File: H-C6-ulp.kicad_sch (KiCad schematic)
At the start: 59 parts, among them J1 USB_C_Receptacle_USB2.0, J2 AFC24-S24FIC-00, J3 S2B-PH-SM4-TB_LF__SN_, Q1 Si1308, Q2 Si2301CDS, U1 ESP32-C6, U2 SGM6029CYG/TR, U3 TP4057-42-SOT26-R, X1 Crystal 40 Mhz 10ppm, Y1 RV-3032-C7

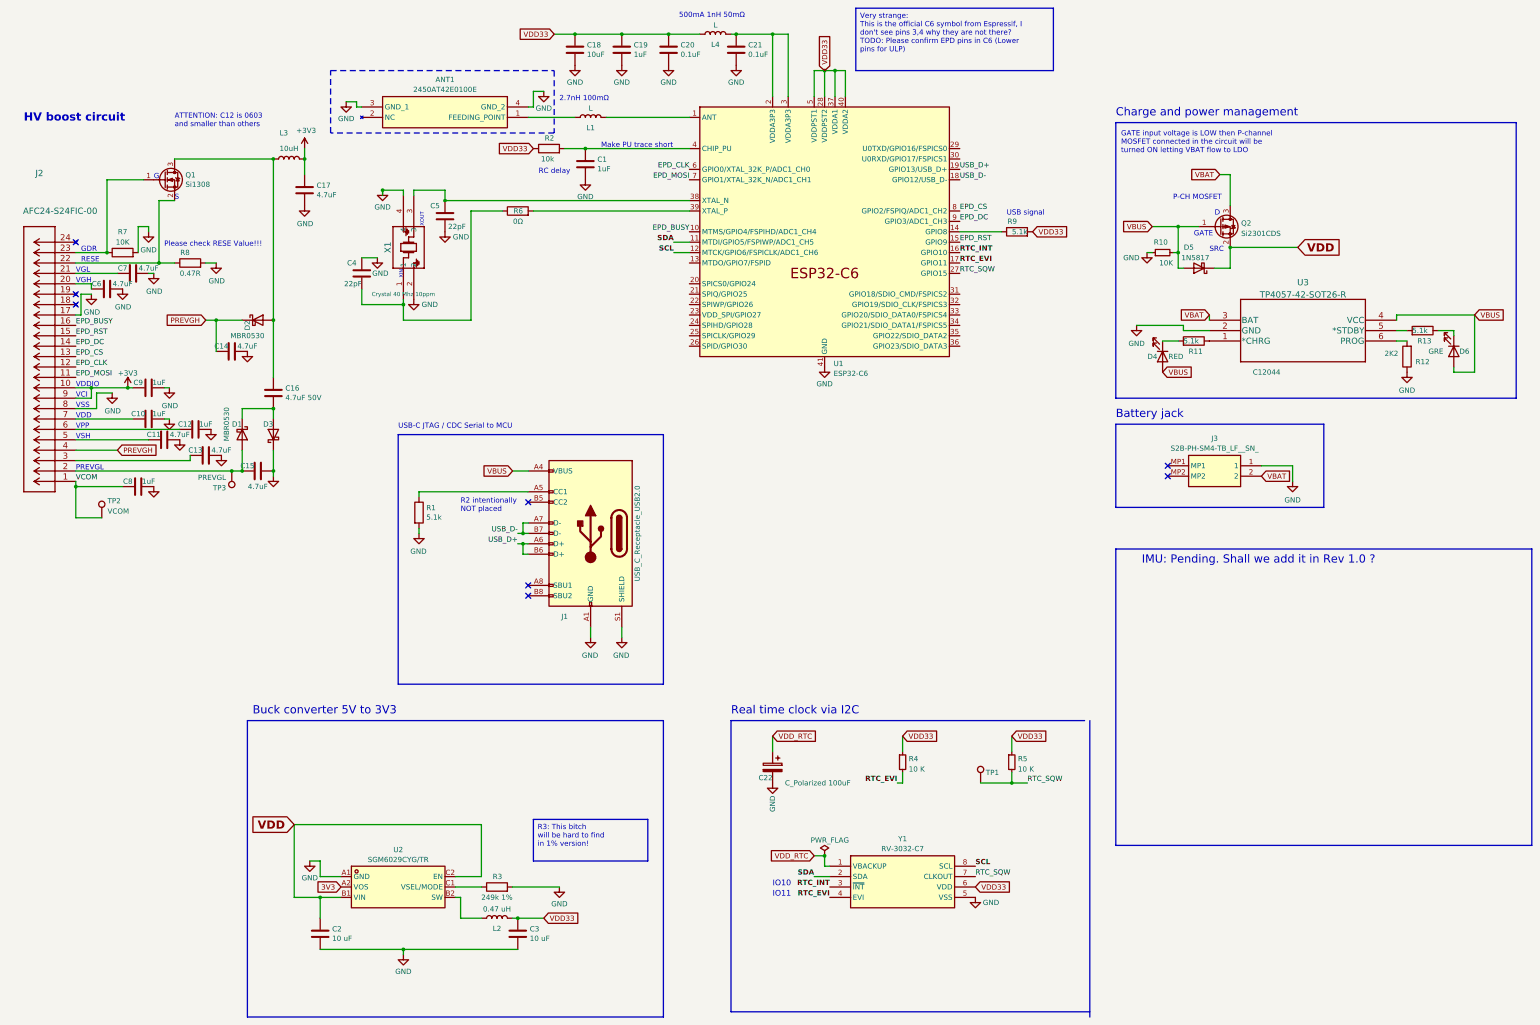
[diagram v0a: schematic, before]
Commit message: First version passing DRC
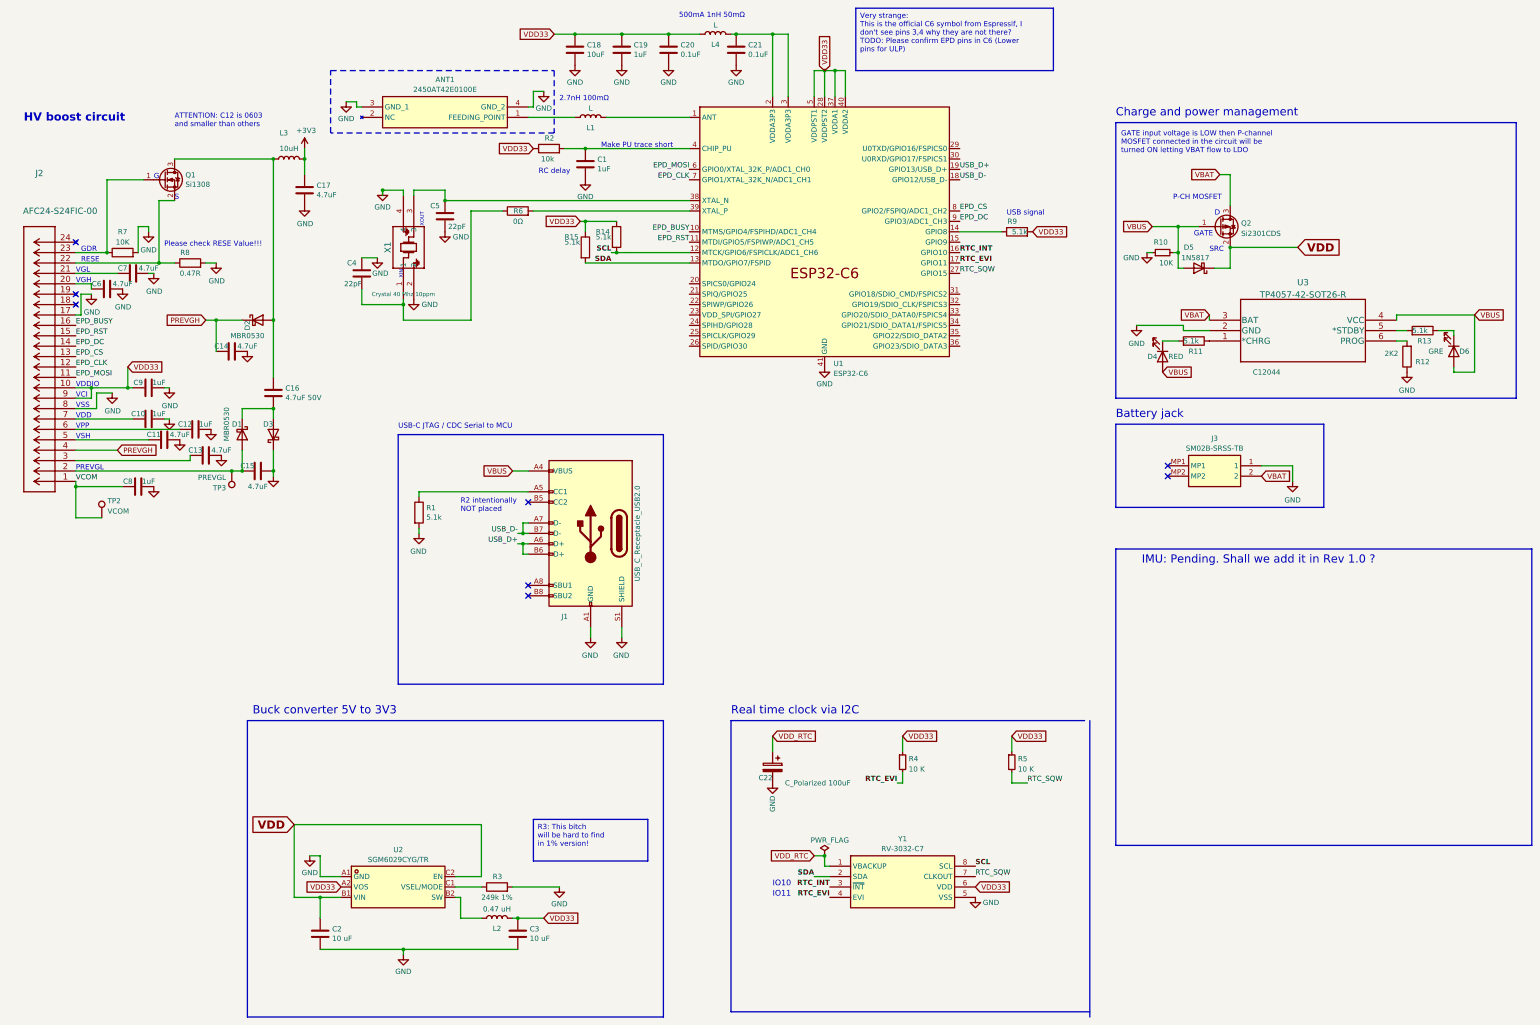
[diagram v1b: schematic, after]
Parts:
- removed TP1: RTC_INT, TestPoint:TestPoint_Pad_1.5x1.5mm, symbol Connector:TestPoint
- added R14, R15: 5.1k, Resistor_SMD:R_0603_1608Metric, symbol Device:R
- J1: footprint Connector_USB:USB_C_Receptacle_HRO_TYPE-C-31-M-12 -> footprints:USB_C_Receptacle_HRO_TYPE-C-31-M-12
- J3: value S2B-PH-SM4-TB_LF__SN_ -> SM02B-SRSS-TB; footprint S2BPHSM4TBLFSN -> footprints:SM02BSRSSTBLFSN; Arrow Part Number S2B-PH-SM4-TB(LF)(SN) -> (none); Arrow Price/Stock https://www.arrow.com/en/products/s2b-ph-sm4-tb-lf-sn/jst-m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 -> (none); Height 6.6 -> (none); LCSC C295747 -> C18337480; Manufacturer_Part_Number S2B-PH-SM4-TB(LF)(SN) -> (none)
- R3: LCSC C5123581 -> C6945215
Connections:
- net 3V3 is gone; now on net VDD33: U2.A2 (VOS)
- net +3V3: no longer C9.2, J2.10, J2.9
- net EPD_CLK: now also U1.7 (GPIO1/XTAL_32K_N/ADC1_CH1); no longer U1.6 (GPIO0/XTAL_32K_P/ADC1_CH0)
- net EPD_MOSI: now also U1.6 (GPIO0/XTAL_32K_P/ADC1_CH0); no longer U1.7 (GPIO1/XTAL_32K_N/ADC1_CH1)
- net EPD_RST: now also U1.11 (MTDI/GPIO5/FSPIWP/ADC1_CH5); no longer U1.15 (GPIO9)
- net SCL: now also R14.2
- net SDA: now also U1.13 (MTDO/GPIO7/FSPID), R15.2; no longer U1.11 (MTDI/GPIO5/FSPIWP/ADC1_CH5)
- net VDD33: now also C9.2, J2.10, J2.9, R14.1, R15.1

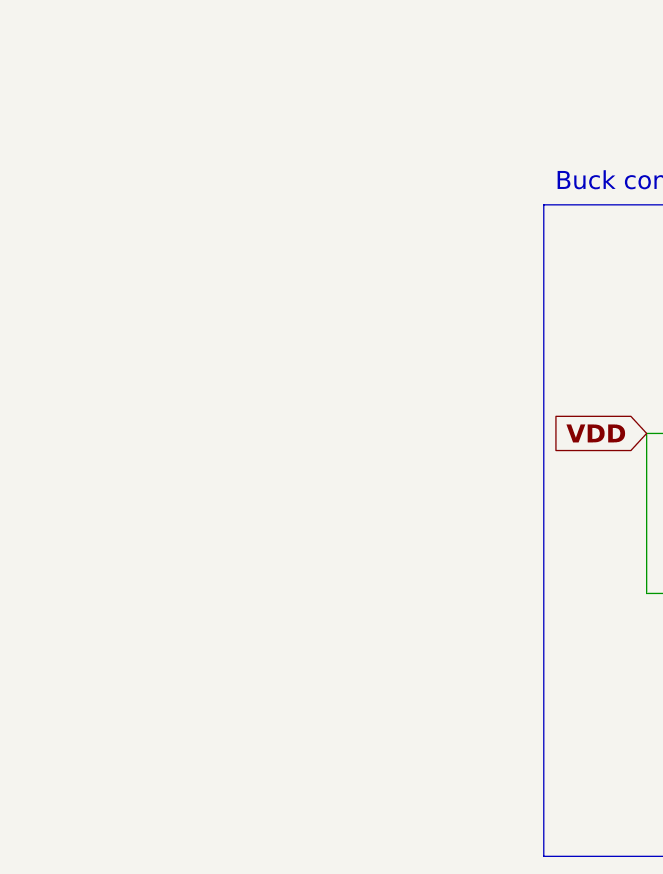
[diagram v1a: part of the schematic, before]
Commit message: Add QWIIC I2c connector
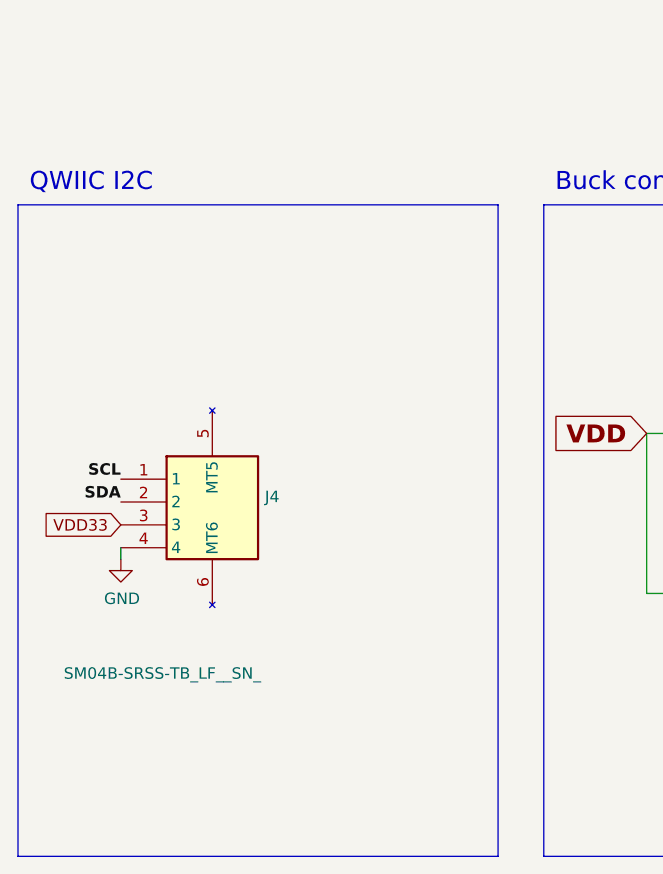
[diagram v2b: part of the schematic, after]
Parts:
- added J4: SM04B-SRSS-TB_LF__SN_, footprints:QWIIC_SM04B-SRSS-TB_LFSN_, symbol QWIIC:SM04B-SRSS-TB_LF__SN_
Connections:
- net GND: now also J4.4
- net SCL: now also J4.1
- net SDA: now also J4.2
- net VDD33: now also J4.3
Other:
- note added: "QWIIC I2C"
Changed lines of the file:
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@@
+    (stroke (width 0) (type default))
+  )
+  (wire (pts (xy 31.75 240.03) (xy 31.75 238.76))
     (stroke (width 0) (type default))
   )
@@
   (wire (pts (xy 334.01 138.43) (xy 326.39 138.43))
     (stroke (width 0) (type default))
+  )
+  (rectangle (start 20.32 200.66) (end 73.66 273.05)
+    (stroke (width 0) (type default))
+    (fill (type none))
   )
   (rectangle (start 78.74 200.66) (end 180.34 273.05)
@@
     (effects (font (size 1.27 1.27)) (justify left bottom))
   )
+  (text "QWIIC I2C" (at 21.59 199.39 0)
+    (effects (font (size 2 2)) (justify left bottom))
+  )
   (text "SRC" (at 313.69 86.36 0)
     (effects (font (size 1.27 1.27)) (justify left bottom))
@@
     (effects (font (size 1.27 1.27) (thickness 0.254) bold (color 0 194 0 1)) (justify right bottom))
   )
+  (label "SDA" (at 31.75 233.68 180) (fields_autoplaced)
+    (effects (font (size 1.27 1.27) (thickness 0.254) bold (color 0 194 0 1)) (justify right bottom))
+  )
   (label "EPD_RST" (at 36.83 106.68 0) (fields_autoplaced)
     (effects (font (size 1.27 1.27)) (justify left bottom))
@@
   (label "EPD_DC" (at 36.83 109.22 0) (fields_autoplaced)
     (effects (font (size 1.27 1.27)) (justify left bottom))
+  )
+  (label "SCL" (at 31.75 231.14 180) (fields_autoplaced)
+    (effects (font (size 1.27 1.27) (thickness 0.254) bold (color 0 194 0 1)) (justify right bottom))
   )
   (label "EPD_MOSI" (at 186.69 66.04 180) (fields_autoplaced)
@@
     )
   )
+  (global_label "VDD33" (shape input) (at 31.75 236.22 180) (fields_autoplaced)
+    (effects (font (size 1.27 1.27)) (justify right))
+    (property "Intersheetrefs" "${INTERSHEET_REFS}" (at 22.7172 236.22 0)
+      (effects (font (size 1.27 1.27)) (justify right) hide)
+    )
+    (property "Referenzen zwischen Schaltplänen" "${INTERSHEET_REFS}" (at 31.75 238.4108 0)
+      (effects (font (size 1.27 1.27)) (justify right) hide)
+    )
+  )
   (global_label "VDD33" (shape input) (at 219.71 41.91 90) (fields_autoplaced)
     (effects (font (size 1.27 1.27)) (justify left))
@@
     (property "Referenzen zwischen Schaltplänen" "${INTERSHEET_REFS}" (at 160.02 80.9308 0)
       (effects (font (size 1.27 1.27)) (justify right) hide)
+    )
+  )
+  (symbol (lib_id "QWIIC:SM04B-SRSS-TB_LF__SN_") (at 31.75 231.14 0) (unit 1)
+    (in_bom yes) (on_board yes) (dnp no)
+    (property "Reference" "J4" (at 47.752 233.1029 0)
+      (effects (font (size 1.27 1.27)) (justify left))
+    )
+    (property "Value" "SM04B-SRSS-TB_LF__SN_" (at 25.4 252.73 0)
+      (effects (font (size 1.27 1.27)) (justify left))
+    )
+    (property "Footprint" "footprints:QWIIC_SM04B-SRSS-TB_LFSN_" (at 48.26 326.06 0)
+      (effects (font (size 1.27 1.27)) (justify left top) hide)
+    )
+    (property "Datasheet" "http://www.jst-mfg.com/product/pdf/eng/eSH.pdf" (at 48.26 426.06 0)
+      (effects (font (size 1.27 1.27)) (justify left top) hide)
+    )
+    (property "Height" "4 mm" (at 48.26 626.06 0)
+      (effects (font (size 1.27 1.27)) (justify left top) hide)
+    )
+    (property "Manufacturer_Name" "JST (JAPAN SOLDERLESS TERMINALS)" (at 48.26 726.06 0)
+      (effects (font (size 1.27 1.27)) (justify left top) hide)
+    )
+    (property "Manufacturer_Part_Number" "SM04B-SRSS-TB(LF)(SN)" (at 48.26 826.06 0)
+      (effects (font (size 1.27 1.27)) (justify left top) hide)
+    )
+    (property "LCSC" "C160404" (at 31.75 231.14 0)
+      (effects (font (size 1.27 1.27)) hide)
+    )
+    (pin "4")
+    (pin "5")
+    (pin "3")
+    (pin "1")
+    (pin "2")
+    (pin "6")
+    (instances
+      (project "H-C6-ulp"
+        (path "/4820ae53-5724-49d2-a676-459cc31081bd"
+          (reference "J4") (unit 1)
+        )
+      )
     )
   )
@@
         )
       )
+    )
+  )
+  (symbol (lib_id "power:GND") (at 31.75 240.03 0) (unit 1)
+    (in_bom yes) (on_board yes) (dnp no)
+    (property "Reference" "#PWR020" (at 31.75 246.38 0)
+      (effects (font (size 1.27 1.27)) hide)
+    )
+    (property "Value" "GND" (at 31.877 244.4242 0)
+      (effects (font (size 1.27 1.27)))
+    )
+    (property "Footprint" "" (at 31.75 240.03 0)
+      (effects (font (size 1.27 1.27)) hide)
+    )
+    (property "Datasheet" "" (at 31.75 240.03 0)
+      (effects (font (size 1.27 1.27)) hide)
+    )
+    (pin "1")
+    (instances
+      (project "H-C6-ulp"
+        (path "/4820ae53-5724-49d2-a676-459cc31081bd"
+          (reference "#PWR020") (unit 1)
+        )
+      )

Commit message: Rev 1.0 is quite ready for last review @bitbank2
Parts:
- added H1, H2, H3, H4: MountingHole, MountingHole:MountingHole_2.2mm_M2, symbol Mechanical:MountingHole
- added TP1: VGH, TestPoint:TestPoint_Pad_D1.5mm, symbol Connector:TestPoint
- J3: value SM02B-SRSS-TB -> SM02B-SRSS-TB(LF)(SN); Height (none) -> 4; LCSC C18337480 -> C160402; Manufacturer_Part_Number (none) -> SM02B-SRSS-TB(LF)(SN)
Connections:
- net PREVGH: now also TP1.1
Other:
- note added: "Mounting"
- note added: "open souce hardware"
